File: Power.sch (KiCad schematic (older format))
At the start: 18 parts, among them P1 24-pin Mini-Fit Jr., SW1 Power Switch

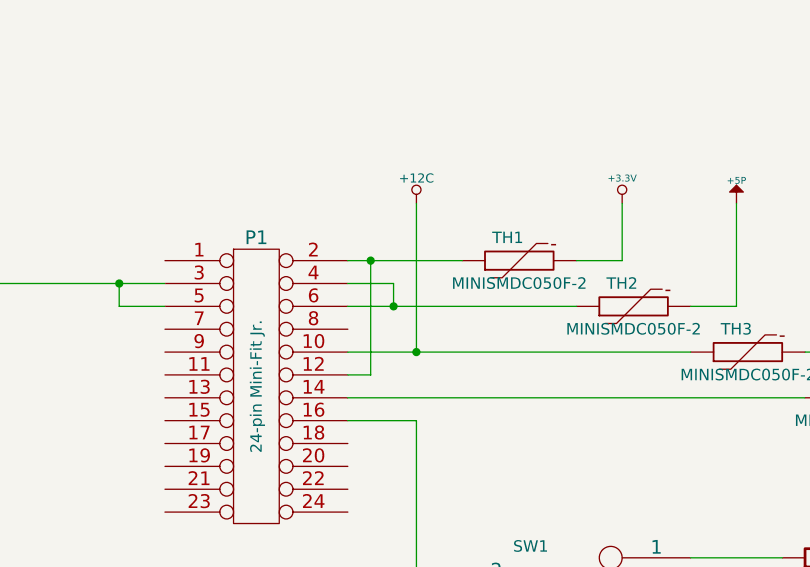
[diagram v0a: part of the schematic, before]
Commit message: Connected remaing nets
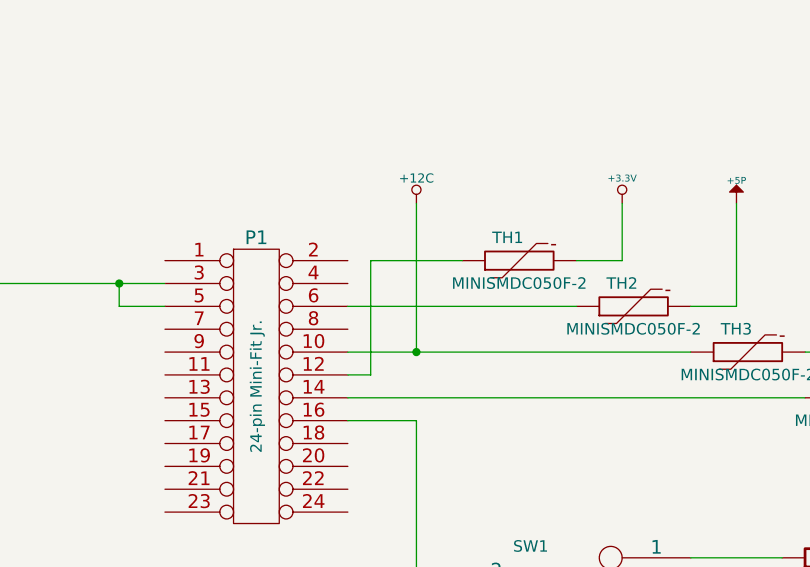
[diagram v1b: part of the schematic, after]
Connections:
- net at P1.12 (P12), TH1.1: no longer P1.2 (P2)
- net at P1.6 (P6), TH2.1: no longer P1.4 (P4)
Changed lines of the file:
@@
 $EndComp
 $Comp
-L GND #PWR06
+L GND #PWR7
 U 1 1 52F29C85
 P 900 2100
-F 0 "#PWR06" H 900 2100 30  0001 C CNN
+F 0 "#PWR7" H 900 2100 30  0001 C CNN
 F 1 "GND" H 900 2030 30  0001 C CNN
 F 2 "" H 900 2100 60  0000 C CNN
@@
 $EndComp
 Wire Wire Line
-	3000 1800 2500 1800
-Wire Wire Line
 	2500 2000 3500 2000
 Wire Wire Line
-	2500 1900 2700 1900
-Wire Wire Line
-	2700 1900 2700 2000
-Connection ~ 2700 2000
-Wire Wire Line
 	3500 1800 3700 1800
 Wire Wire Line
@@
 	4700 2200 4700 1550
 $Comp
-L +12P #PWR07
+L +12P #PWR17
 U 1 1 52F29CC3
 P 4700 1550
-F 0 "#PWR07" H 4700 1520 30  0001 C CNN
+F 0 "#PWR17" H 4700 1520 30  0001 C CNN
 F 1 "+12P" H 4700 1650 30  0000 C CNN
 F 2 "" H 4700 1550 60  0000 C CNN
@@
 	5200 2400 5200 1550
 $Comp
-L -12P #PWR08
+L -12P #PWR19
 U 1 1 52F29CCB
 P 5200 1550
-F 0 "#PWR08" H 5200 1680 20  0001 C CNN
+F 0 "#PWR19" H 5200 1680 20  0001 C CNN
 F 1 "-12P" H 5200 1650 30  0000 C CNN
 F 2 "" H 5200 1550 60  0000 C CNN
@@
 	4300 3300 4300 3500
 $Comp
-L GND #PWR09
+L GND #PWR12
 U 1 1 52F29CDA
 P 4300 3500
-F 0 "#PWR09" H 4300 3500 30  0001 C CNN
+F 0 "#PWR12" H 4300 3500 30  0001 C CNN
 F 1 "GND" H 4300 3430 30  0001 C CNN
 F 2 "" H 4300 3500 60  0000 C CNN
@@
 	5100 3100 5100 2900
 $Comp
-L +3.3V #PWR010
+L +3.3V #PWR18
 U 1 1 52F29CE9
 P 5100 2900
-F 0 "#PWR010" H 5100 2860 30  0001 C CNN
+F 0 "#PWR18" H 5100 2860 30  0001 C CNN
 F 1 "+3.3V" H 5100 3010 30  0000 C CNN
 F 2 "" H 5100 2900 60  0000 C CNN
@@
 $EndComp
 $Comp
-L +12P #PWR011
+L +12P #PWR21
 U 1 1 52F29CEF
 P 6600 2150
-F 0 "#PWR011" H 6600 2120 30  0001 C CNN
+F 0 "#PWR21" H 6600 2120 30  0001 C CNN
 F 1 "+12P" H 6600 2250 30  0000 C CNN
 F 2 "" H 6600 2150 60  0000 C CNN
@@
 $EndComp
 $Comp
-L -12P #PWR012
+L -12P #PWR22
 U 1 1 52F29CF5
 P 6600 3750
-F 0 "#PWR012" H 6600 3880 20  0001 C CNN
+F 0 "#PWR22" H 6600 3880 20  0001 C CNN
 F 1 "-12P" H 6600 3850 30  0000 C CNN
 F 2 "" H 6600 3750 60  0000 C CNN
@@
 $EndComp
 $Comp
-L GND #PWR013
+L GND #PWR23
 U 1 1 52F29CFB
 P 7500 3100
-F 0 "#PWR013" H 7500 3100 30  0001 C CNN
+F 0 "#PWR23" H 7500 3100 30  0001 C CNN
 F 1 "GND" H 7500 3030 30  0001 C CNN
 F 2 "" H 7500 3100 60  0000 C CNN
@@
 Connection ~ 7800 3550
 $Comp
-L +12V #PWR014
+L +12V #PWR26
 U 1 1 52F29D29
 P 8250 2150
-F 0 "#PWR014" H 8250 2100 20  0001 C CNN
+F 0 "#PWR26" H 8250 2100 20  0001 C CNN
 F 1 "+12V" H 8250 2250 30  0000 C CNN
 F 2 "" H 8250 2150 60  0000 C CNN
@@
 $EndComp
 $Comp
-L -12V #PWR015
+L -12V #PWR27
 U 1 1 52F29D2F
 P 8250 3750
-F 0 "#PWR015" H 8250 3880 20  0001 C CNN
+F 0 "#PWR27" H 8250 3880 20  0001 C CNN
 F 1 "-12V" H 8250 3850 30  0000 C CNN
 F 2 "" H 8250 3750 60  0000 C CNN
@@
 	2800 2200 2800 1550
 $Comp
-L +12C #PWR016
+L +12C #PWR8
 U 1 1 52FBE7EF
 P 2800 1550
-F 0 "#PWR016" H 2800 1520 30  0001 C CNN
+F 0 "#PWR8" H 2800 1520 30  0001 C CNN
 F 1 "+12C" H 2800 1660 40  0000 C CNN
 F 2 "" H 2800 1550 60  0000 C CNN
@@
 $EndComp
 $Comp
-L +5V #PWR017
+L +5V #PWR25
 U 1 1 530A2195
 P 8250 850
-F 0 "#PWR017" H 8250 940 20  0001 C CNN
+F 0 "#PWR25" H 8250 940 20  0001 C CNN
 F 1 "+5V" H 8250 940 30  0000 C CNN
 F 2 "" H 8250 850 60  0000 C CNN
@@
 $EndComp
 $Comp
-L GND #PWR018
+L GND #PWR24
 U 1 1 530A21B1
 P 7800 1750
-F 0 "#PWR018" H 7800 1750 30  0001 C CNN
+F 0 "#PWR24" H 7800 1750 30  0001 C CNN
 F 1 "GND" H 7800 1680 30  0001 C CNN
 F 2 "" H 7800 1750 60  0000 C CNN
@@
 Wire Wire Line
 	2600 2300 2600 1800
-Connection ~ 2600 1800
 $Comp
 L +5P #PWR11
@@
 $EndComp
 $Comp
-L +3.3V #PWR019
+L +3.3V #PWR10
 U 1 1 52F29C8B
 P 3700 1550
-F 0 "#PWR019" H 3700 1510 30  0001 C CNN
+F 0 "#PWR10" H 3700 1510 30  0001 C CNN
 F 1 "+3.3V" H 3700 1660 30  0000 C CNN
 F 2 "" H 3700 1550 60  0000 C CNN
@@
 	3000 5300 3000 7200
 $Comp
-L GND #PWR020
+L GND #PWR9
 U 1 1 5316543C
 P 3000 7200
-F 0 "#PWR020" H 3000 7200 30  0001 C CNN
+F 0 "#PWR9" H 3000 7200 30  0001 C CNN
 F 1 "GND" H 3000 7130 30  0001 C CNN
 F 2 "" H 3000 7200 60  0000 C CNN
@@
 	4400 6900 4400 7100
 $Comp
-L AGND #PWR021
+L AGND #PWR13
 U 1 1 5316559F
 P 4400 5900
-F 0 "#PWR021" H 4400 5900 40  0001 C CNN
+F 0 "#PWR13" H 4400 5900 40  0001 C CNN
 F 1 "AGND" H 4400 5830 50  0000 C CNN
 F 2 "" H 4400 5900 60  0000 C CNN
@@
 $EndComp
 $Comp
-L GND_PWR #PWR022
+L GND_PWR #PWR14
 U 1 1 531655B3
 P 4400 6300
-F 0 "#PWR022" H 4400 6300 30  0001 C CNN
+F 0 "#PWR14" H 4400 6300 30  0001 C CNN
 F 1 "GND_PWR" H 4400 6230 30  0000 C CNN
 F 2 "" H 4400 6300 60  0000 C CNN
@@
 $EndComp
 $Comp
-L GND_LED #PWR023
+L GND_LED #PWR15
 U 1 1 531655C7
 P 4400 6700
-F 0 "#PWR023" H 4400 6700 30  0001 C CNN
+F 0 "#PWR15" H 4400 6700 30  0001 C CNN
 F 1 "GND_LED" H 4400 6630 30  0000 C CNN
 F 2 "" H 4400 6700 60  0000 C CNN
@@
 $EndComp
 $Comp
-L GND_RELAY #PWR024
+L GND_RELAY #PWR16
 U 1 1 531655DB
 P 4400 7100
-F 0 "#PWR024" H 4400 7100 30  0001 C CNN
+F 0 "#PWR16" H 4400 7100 30  0001 C CNN
 F 1 "GND_RELAY" H 4400 7030 30  0000 C CNN
 F 2 "" H 4400 7100 60  0000 C CNN
@@
 $EndComp
 Connection ~ 3000 5700
+Wire Wire Line
+	2600 1800 3000 1800
 $EndSCHEMATC

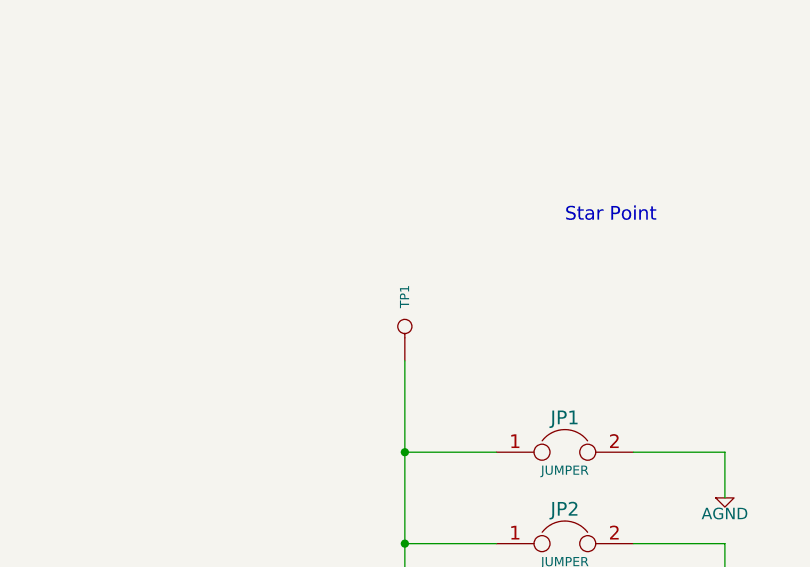
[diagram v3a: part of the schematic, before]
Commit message: Test points added, silk screen updates
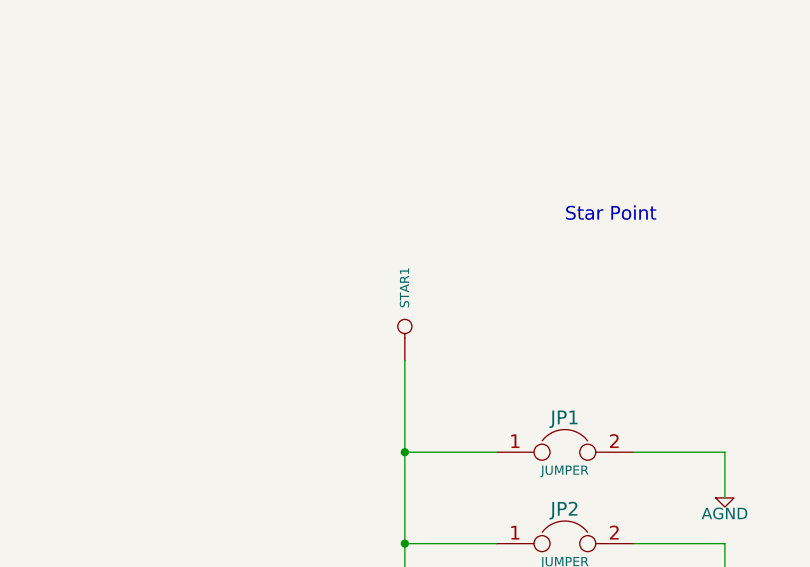
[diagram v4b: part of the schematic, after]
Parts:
- renumbered TP1 to STAR1
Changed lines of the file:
@@
 $EndComp
 $Comp
-L GND #PWR7
+L GND #PWR06
 U 1 1 52F29C85
 P 900 2100
-F 0 "#PWR7" H 900 2100 30  0001 C CNN
+F 0 "#PWR06" H 900 2100 30  0001 C CNN
 F 1 "GND" H 900 2030 30  0001 C CNN
 F 2 "" H 900 2100 60  0000 C CNN
@@
 	4700 2200 4700 1550
 $Comp
-L +12P #PWR17
+L +12P #PWR07
 U 1 1 52F29CC3
 P 4700 1550
-F 0 "#PWR17" H 4700 1520 30  0001 C CNN
+F 0 "#PWR07" H 4700 1520 30  0001 C CNN
 F 1 "+12P" H 4700 1650 30  0000 C CNN
 F 2 "" H 4700 1550 60  0000 C CNN
@@
 	5200 2400 5200 1550
 $Comp
-L -12P #PWR19
+L -12P #PWR08
 U 1 1 52F29CCB
 P 5200 1550
-F 0 "#PWR19" H 5200 1680 20  0001 C CNN
+F 0 "#PWR08" H 5200 1680 20  0001 C CNN
 F 1 "-12P" H 5200 1650 30  0000 C CNN
 F 2 "" H 5200 1550 60  0000 C CNN
@@
 	4300 3300 4300 3500
 $Comp
-L GND #PWR12
+L GND #PWR09
 U 1 1 52F29CDA
 P 4300 3500
-F 0 "#PWR12" H 4300 3500 30  0001 C CNN
+F 0 "#PWR09" H 4300 3500 30  0001 C CNN
 F 1 "GND" H 4300 3430 30  0001 C CNN
 F 2 "" H 4300 3500 60  0000 C CNN
@@
 	5100 3100 5100 2900
 $Comp
-L +3.3V #PWR18
+L +3.3V #PWR010
 U 1 1 52F29CE9
 P 5100 2900
-F 0 "#PWR18" H 5100 2860 30  0001 C CNN
+F 0 "#PWR010" H 5100 2860 30  0001 C CNN
 F 1 "+3.3V" H 5100 3010 30  0000 C CNN
 F 2 "" H 5100 2900 60  0000 C CNN
@@
 $EndComp
 $Comp
-L +12P #PWR21
+L +12P #PWR011
 U 1 1 52F29CEF
 P 6600 2150
-F 0 "#PWR21" H 6600 2120 30  0001 C CNN
+F 0 "#PWR011" H 6600 2120 30  0001 C CNN
 F 1 "+12P" H 6600 2250 30  0000 C CNN
 F 2 "" H 6600 2150 60  0000 C CNN
@@
 $EndComp
 $Comp
-L -12P #PWR22
+L -12P #PWR012
 U 1 1 52F29CF5
 P 6600 3750
-F 0 "#PWR22" H 6600 3880 20  0001 C CNN
+F 0 "#PWR012" H 6600 3880 20  0001 C CNN
 F 1 "-12P" H 6600 3850 30  0000 C CNN
 F 2 "" H 6600 3750 60  0000 C CNN
@@
 $EndComp
 $Comp
-L GND #PWR23
+L GND #PWR013
 U 1 1 52F29CFB
 P 7500 3100
-F 0 "#PWR23" H 7500 3100 30  0001 C CNN
+F 0 "#PWR013" H 7500 3100 30  0001 C CNN
 F 1 "GND" H 7500 3030 30  0001 C CNN
 F 2 "" H 7500 3100 60  0000 C CNN
@@
 Connection ~ 7800 3550
 $Comp
-L +12V #PWR26
+L +12V #PWR014
 U 1 1 52F29D29
 P 8250 2150
-F 0 "#PWR26" H 8250 2100 20  0001 C CNN
+F 0 "#PWR014" H 8250 2100 20  0001 C CNN
 F 1 "+12V" H 8250 2250 30  0000 C CNN
 F 2 "" H 8250 2150 60  0000 C CNN
@@
 $EndComp
 $Comp
-L -12V #PWR27
+L -12V #PWR015
 U 1 1 52F29D2F
 P 8250 3750
-F 0 "#PWR27" H 8250 3880 20  0001 C CNN
+F 0 "#PWR015" H 8250 3880 20  0001 C CNN
 F 1 "-12V" H 8250 3850 30  0000 C CNN
 F 2 "" H 8250 3750 60  0000 C CNN
@@
 	2800 2200 2800 1550
 $Comp
-L +12C #PWR8
+L +12C #PWR016
 U 1 1 52FBE7EF
 P 2800 1550
-F 0 "#PWR8" H 2800 1520 30  0001 C CNN
+F 0 "#PWR016" H 2800 1520 30  0001 C CNN
 F 1 "+12C" H 2800 1660 40  0000 C CNN
 F 2 "" H 2800 1550 60  0000 C CNN
@@
 $EndComp
 $Comp
-L +5V #PWR25
+L +5V #PWR017
 U 1 1 530A2195
 P 8250 850
-F 0 "#PWR25" H 8250 940 20  0001 C CNN
+F 0 "#PWR017" H 8250 940 20  0001 C CNN
 F 1 "+5V" H 8250 940 30  0000 C CNN
 F 2 "" H 8250 850 60  0000 C CNN
@@
 $EndComp
 $Comp
-L GND #PWR24
+L GND #PWR018
 U 1 1 530A21B1
 P 7800 1750
-F 0 "#PWR24" H 7800 1750 30  0001 C CNN
+F 0 "#PWR018" H 7800 1750 30  0001 C CNN
 F 1 "GND" H 7800 1680 30  0001 C CNN
 F 2 "" H 7800 1750 60  0000 C CNN
@@
 $EndComp
 $Comp
-L CONN_1 TP1
+L CONN_1 STAR1
 U 1 1 53163E2C
 P 3000 5150
-F 0 "TP1" H 3080 5150 40  0000 L CNN
+F 0 "STAR1" H 3080 5150 40  0000 L CNN
 F 1 "CONN_1" H 3000 5205 30  0001 C CNN
 F 2 "" H 3000 5150 60  0000 C CNN
@@
 $EndComp
 $Comp
-L +3.3V #PWR10
+L +3.3V #PWR019
 U 1 1 52F29C8B
 P 3700 1550
-F 0 "#PWR10" H 3700 1510 30  0001 C CNN
+F 0 "#PWR019" H 3700 1510 30  0001 C CNN
 F 1 "+3.3V" H 3700 1660 30  0000 C CNN
 F 2 "" H 3700 1550 60  0000 C CNN
@@
 	3000 5300 3000 7200
 $Comp
-L GND #PWR9
+L GND #PWR020
 U 1 1 5316543C
 P 3000 7200
-F 0 "#PWR9" H 3000 7200 30  0001 C CNN
+F 0 "#PWR020" H 3000 7200 30  0001 C CNN
 F 1 "GND" H 3000 7130 30  0001 C CNN
 F 2 "" H 3000 7200 60  0000 C CNN
@@
 	4400 6900 4400 7100
 $Comp
-L AGND #PWR13
+L AGND #PWR021
 U 1 1 5316559F
 P 4400 5900
-F 0 "#PWR13" H 4400 5900 40  0001 C CNN
+F 0 "#PWR021" H 4400 5900 40  0001 C CNN
 F 1 "AGND" H 4400 5830 50  0000 C CNN
 F 2 "" H 4400 5900 60  0000 C CNN
@@
 $EndComp
 $Comp
-L GND_PWR #PWR14
+L GND_PWR #PWR022
 U 1 1 531655B3
 P 4400 6300
-F 0 "#PWR14" H 4400 6300 30  0001 C CNN
+F 0 "#PWR022" H 4400 6300 30  0001 C CNN
 F 1 "GND_PWR" H 4400 6230 30  0000 C CNN
 F 2 "" H 4400 6300 60  0000 C CNN
@@
 $EndComp
 $Comp
-L GND_LED #PWR15
+L GND_LED #PWR023
 U 1 1 531655C7
 P 4400 6700
-F 0 "#PWR15" H 4400 6700 30  0001 C CNN
+F 0 "#PWR023" H 4400 6700 30  0001 C CNN
 F 1 "GND_LED" H 4400 6630 30  0000 C CNN
 F 2 "" H 4400 6700 60  0000 C CNN
@@
 $EndComp
 $Comp
-L GND_RELAY #PWR16
+L GND_RELAY #PWR024
 U 1 1 531655DB
 P 4400 7100
-F 0 "#PWR16" H 4400 7100 30  0001 C CNN
+F 0 "#PWR024" H 4400 7100 30  0001 C CNN
 F 1 "GND_RELAY" H 4400 7030 30  0000 C CNN
 F 2 "" H 4400 7100 60  0000 C CNN

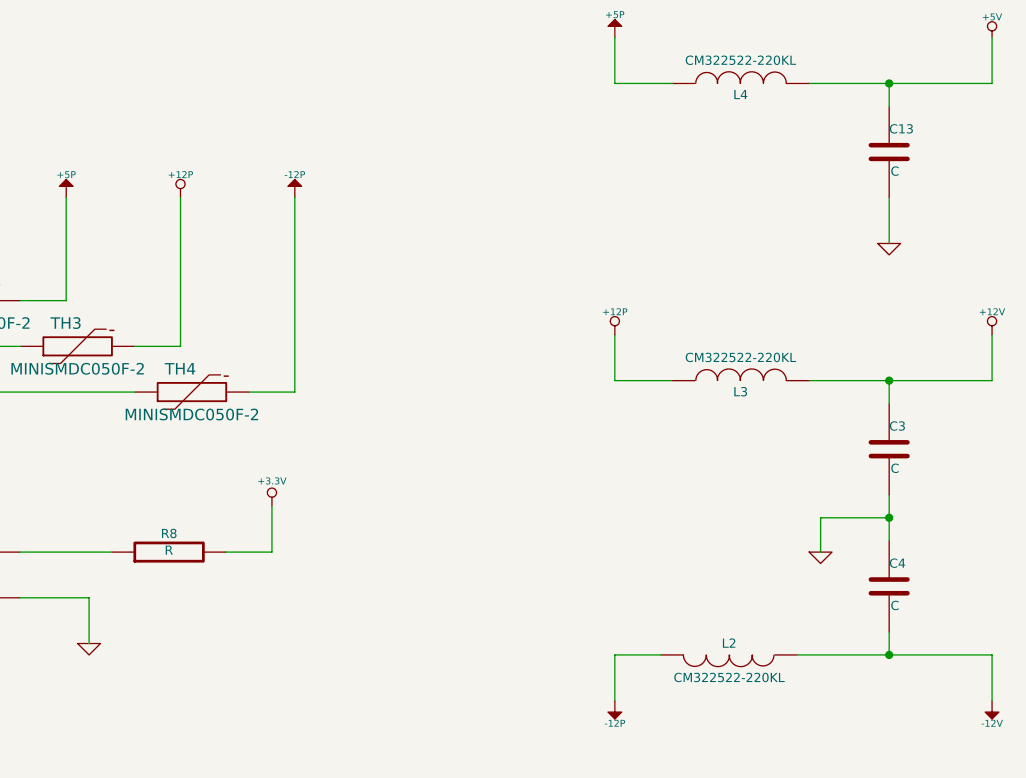
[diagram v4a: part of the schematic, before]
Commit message: Assigned values to passives in Arduino, power adjustment monitor, relay and terminal block schematics
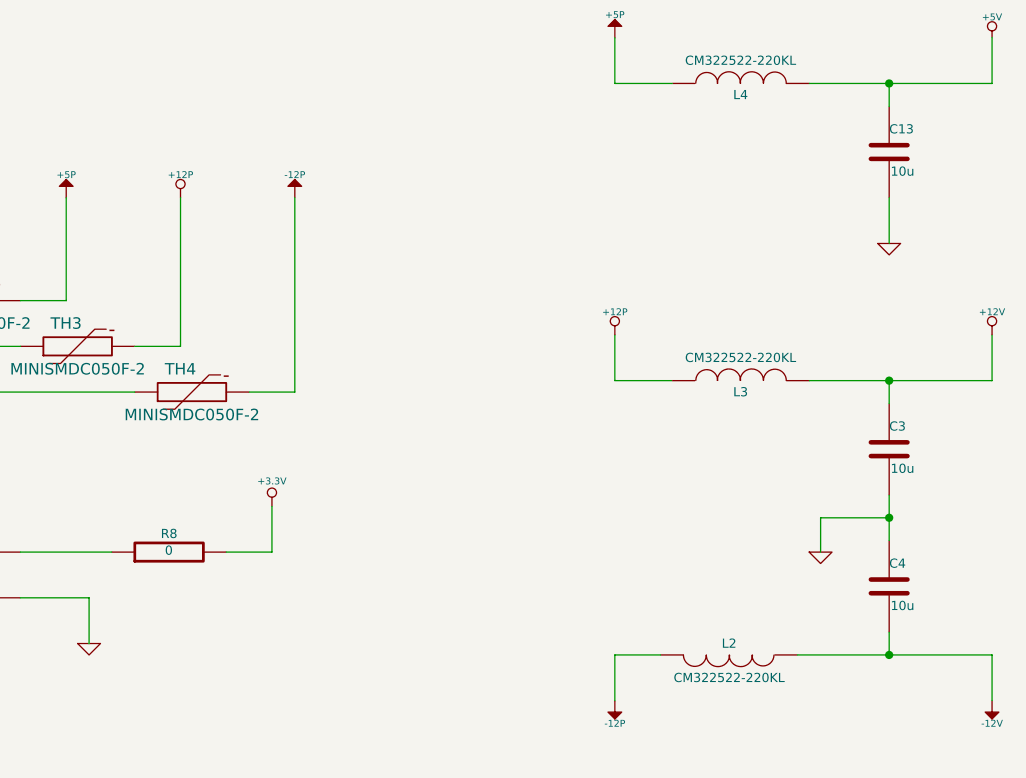
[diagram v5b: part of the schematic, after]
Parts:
- C13, C3, C4: value C -> 10u
- R8: value R -> 0
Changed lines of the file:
@@
 P 4650 3100
 F 0 "R8" V 4730 3100 40  0000 C CNN
-F 1 "R" V 4657 3101 40  0000 C CNN
+F 1 "0" V 4657 3101 40  0000 C CNN
 F 2 "" V 4580 3100 30  0000 C CNN
 F 3 "" H 4650 3100 30  0000 C CNN
@@
 P 7800 3250
 F 0 "C4" H 7800 3350 40  0000 L CNN
-F 1 "C" H 7806 3165 40  0000 L CNN
+F 1 "10u" H 7806 3165 40  0000 L CNN
 F 2 "" H 7838 3100 30  0000 C CNN
 F 3 "" H 7800 3250 60  0000 C CNN
@@
 P 7800 2650
 F 0 "C3" H 7800 2750 40  0000 L CNN
-F 1 "C" H 7806 2565 40  0000 L CNN
+F 1 "10u" H 7806 2565 40  0000 L CNN
 F 2 "" H 7838 2500 30  0000 C CNN
 F 3 "" H 7800 2650 60  0000 C CNN
@@
 P 7800 1350
 F 0 "C13" H 7800 1450 40  0000 L CNN
-F 1 "C" H 7806 1265 40  0000 L CNN
+F 1 "10u" H 7806 1265 40  0000 L CNN
 F 2 "" H 7838 1200 30  0000 C CNN
 F 3 "" H 7800 1350 60  0000 C CNN
